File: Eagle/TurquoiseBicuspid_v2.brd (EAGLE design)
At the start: 56 x 56 mm, 19 parts, among them J0 0Ω, J2 0Ω

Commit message: board design v2
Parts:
- moved C2 0.20 mm to (34.7, 46.2)
- moved R5 0.20 mm to (36.9, 46.2)
- moved R2 0.10 mm to (23.9, 34.7)
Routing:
- net GND: track 244.4 -> 299.3 mm
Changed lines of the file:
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@@
 <wire x1="56" y1="56" x2="0" y2="56" width="0" layer="20"/>
 <wire x1="0" y1="56" x2="0" y2="0" width="0" layer="20"/>
-<text x="3.6" y="15.4" size="1.27" layer="21">Jared De La Cruz
+<text x="6.5" y="11.3" size="1.27" layer="21">Jared De La Cruz
 jared@jareddlc.com
 @jareddlc</text>
@@
 <attribute name="MF" value="" x="-28.58" y="11.45" size="1.778" layer="27" rot="R270" display="off"/>
 <attribute name="OC_FARNELL" value="unknown" x="-28.58" y="11.45" size="1.778" layer="27" rot="R270" display="off"/>
-<attribute name="NAME" x="10.765" y="27.235" size="1.27" layer="25"/>
+<attribute name="NAME" x="11.365" y="27.635" size="1.27" layer="25"/>
 </element>
 <element name="R1" library="rcl" package="M1206" value="330Ω" x="23.9" y="31.59" smashed="yes" rot="R180">
-<attribute name="NAME" x="22.67" y="34.22" size="1.27" layer="25" rot="R180"/>
-<attribute name="VALUE" x="27.27" y="34.23" size="1.27" layer="27" rot="R180"/>
-</element>
-<element name="R2" library="rcl" package="M1206" value="330Ω" x="23.9" y="34.6" smashed="yes">
-<attribute name="NAME" x="20.73" y="35.97" size="1.27" layer="25"/>
-<attribute name="VALUE" x="23.53" y="35.96" size="1.27" layer="27"/>
+<attribute name="NAME" x="21.77" y="30.02" size="1.27" layer="25" rot="R180"/>
+<attribute name="VALUE" x="26.17" y="30.03" size="1.27" layer="27" rot="R180"/>
+</element>
+<element name="R2" library="rcl" package="M1206" value="330Ω" x="23.9" y="34.7" smashed="yes">
+<attribute name="NAME" x="19.63" y="32.57" size="1.27" layer="25"/>
+<attribute name="VALUE" x="22.43" y="32.56" size="1.27" layer="27"/>
 </element>
 <element name="R3" library="rcl" package="M1206" value="330Ω" x="32.19" y="33.1" smashed="yes" rot="R90">
-<attribute name="NAME" x="30.77" y="36.72" size="1.27" layer="25" rot="R180"/>
-<attribute name="VALUE" x="35.57" y="36.73" size="1.27" layer="27" rot="R180"/>
+<attribute name="NAME" x="31.07" y="30.52" size="1.27" layer="25" rot="R180"/>
+<attribute name="VALUE" x="35.57" y="30.53" size="1.27" layer="27" rot="R180"/>
 </element>
 <element name="S1" library="switch-omron" package="B3F-10XX" value="" x="6.35" y="4.12">
@@
 </element>
 <element name="R4" library="rcl" package="R1206" value="10kΩ" x="21.61" y="48.55" smashed="yes" rot="R270">
-<attribute name="NAME" x="16.88" y="51.28" size="1.27" layer="25"/>
-<attribute name="VALUE" x="19.28" y="51.27" size="1.27" layer="27"/>
+<attribute name="NAME" x="18.38" y="44.98" size="1.27" layer="25"/>
+<attribute name="VALUE" x="20.88" y="44.97" size="1.27" layer="27"/>
 </element>
 <element name="S2" library="switch-omron" package="B3F-10XX" value="" x="49.72" y="4.12">
@@
 </element>
 <element name="J0" library="rcl" package="R1206" value="0Ω" x="17.31" y="26.4" smashed="yes">
-<attribute name="NAME" x="14.53" y="24.24" size="1.27" layer="25" rot="R90"/>
-<attribute name="VALUE" x="14.54" y="26.64" size="1.27" layer="27" rot="R90"/>
+<attribute name="NAME" x="16.66" y="24.93" size="1.27" layer="25" rot="R180"/>
+<attribute name="VALUE" x="19.26" y="24.84" size="1.27" layer="27" rot="R180"/>
 </element>
 <element name="J2" library="rcl" package="R1206" value="0Ω" x="28" y="50.8" smashed="yes" rot="R90">
-<attribute name="NAME" x="34.17" y="52.53" size="1.27" layer="25" rot="R180"/>
-<attribute name="VALUE" x="36.87" y="52.54" size="1.27" layer="27" rot="R180"/>
-</element>
-<element name="R5" library="resistor" package="R1206" value="10kΩ" x="36.9" y="46" rot="R270"/>
-<element name="R6" library="resistor" package="R1206" value="10kΩ" x="37.9" y="41.1" rot="R270"/>
+<attribute name="NAME" x="27.37" y="47.53" size="1.27" layer="25" rot="R180"/>
+<attribute name="VALUE" x="29.87" y="47.54" size="1.27" layer="27" rot="R180"/>
+</element>
+<element name="R5" library="resistor" package="R1206" value="10kΩ" x="36.9" y="46.2" smashed="yes" rot="R270">
+<attribute name="NAME" x="36.003" y="49.143" size="1.27" layer="25"/>
+<attribute name="VALUE" x="38.403" y="49.187" size="1.27" layer="27"/>
+</element>
+<element name="R6" library="resistor" package="R1206" value="10kΩ" x="37.9" y="41.1" smashed="yes" rot="R270">
+<attribute name="NAME" x="35.203" y="37.243" size="1.27" layer="25"/>
+<attribute name="VALUE" x="35.003" y="35.787" size="1.27" layer="27"/>
+</element>
 <element name="HM-10" library="HM-10" package="HM-10" value="HM-10BOARD" x="47.6" y="41.1"/>
 <element name="USB" library="fci_micro_usb" package="10118192-0001LF" value="10118192-0001LF" x="0" y="30.5" rot="R270"/>
-<element name="ATTINY85" library="attiny85" package="ATTINY85" value="ATTINY85SU" x="28.7" y="40.4" rot="R270"/>
-<element name="C2" library="rcl" package="C1206" value="0.1µf" x="34.7" y="46" rot="R90"/>
-<element name="C3" library="rcl" package="C1206" value="10µf" x="8.7" y="30.5" rot="R270"/>
+<element name="ATTINY85" library="attiny85" package="ATTINY85" value="ATTINY85SU" x="28.7" y="40.4" smashed="yes" rot="R270">
+<attribute name="NAME" x="22.96" y="43.167" size="1.4224" layer="25" ratio="9"/>
+<attribute name="VALUE" x="21.56" y="36.2042" size="1.4224" layer="27" ratio="9"/>
+</element>
+<element name="C2" library="rcl" package="C1206" value="0.1µf" x="34.7" y="46.2" smashed="yes" rot="R90">
+<attribute name="NAME" x="33.37" y="47.53" size="1.27" layer="25" rot="R180"/>
+<attribute name="VALUE" x="33.77" y="46.14" size="1.27" layer="27" rot="R180"/>
+</element>
+<element name="C3" library="rcl" package="C1206" value="10µf" x="8.7" y="30.5" smashed="yes" rot="R270">
+<attribute name="NAME" x="5.03" y="26.67" size="1.27" layer="25"/>
+<attribute name="VALUE" x="7.53" y="26.66" size="1.27" layer="27"/>
+</element>
 </elements>
 <signals>
@@
 <wire x1="11.6" y1="29.1" x2="11.6" y2="30.5" width="0.4064" layer="1"/>
 <wire x1="13.2999" y1="30.5" x2="11.6" y2="30.5" width="0.4064" layer="1"/>
-<wire x1="34.7" y1="47.4" x2="35.1" y2="51.1" width="0.4064" layer="1"/>
-<wire x1="35.1" y1="51.1" x2="35.1" y2="54.6" width="0" layer="19" extent="1-16"/>
-<wire x1="36.9" y1="47.422" x2="38.8" y2="51.1" width="0" layer="19" extent="1-16"/>
-<wire x1="38.8" y1="51.1" x2="35.1" y2="51.1" width="0.4064" layer="1"/>
+<wire x1="34.7" y1="47.6" x2="34.7" y2="50.9" width="0.4064" layer="1"/>
 <wire x1="19.3" y1="26.4" x2="19.3" y2="28.1" width="0.4064" layer="1"/>
 <wire x1="19.3" y1="28.1" x2="19.3" y2="48.5594" width="0.4064" layer="1"/>
@@
 <wire x1="23.9" y1="38.495" x2="23.9" y2="28.1" width="0.4064" layer="1"/>
 <wire x1="23.9" y1="38.495" x2="25.37" y2="38.495" width="0.4064" layer="1"/>
-<wire x1="24.7388" y1="48.5594" x2="34.7" y2="47.4" width="0" layer="19" extent="1-1"/>
+<wire x1="37.9" y1="42.522" x2="38.4" y2="43.122" width="0.4064" layer="1"/>
+<wire x1="38.4" y1="43.122" x2="38.4" y2="50.9" width="0.4064" layer="1"/>
+<wire x1="36.9" y1="47.622" x2="36.9" y2="50.9" width="0.4064" layer="1"/>
+<wire x1="34.7" y1="50.9" x2="36.9" y2="50.9" width="0.4064" layer="1"/>
+<wire x1="36.9" y1="50.9" x2="38.4" y2="50.9" width="0.4064" layer="1"/>
+<wire x1="38.4" y1="50.9" x2="46.8" y2="50.9" width="0.4064" layer="1"/>
+<wire x1="46.8" y1="50.9" x2="46.8" y2="23.1" width="0.4064" layer="1"/>
+<wire x1="46.8" y1="23.1" x2="40.1" y2="23.1" width="0.4064" layer="1"/>
 <wire x1="15.888" y1="26.4" x2="18.732" y2="26.4" width="0" layer="19" extent="1-1"/>
-<wire x1="37.9" y1="42.522" x2="38.4" y2="43.122" width="0.4064" layer="1"/>
-<wire x1="38.4" y1="43.122" x2="38.4" y2="48.5" width="0.4064" layer="1"/>
-<wire x1="38.4" y1="48.5" x2="37.676609375" y2="48.92535" width="0" layer="19" extent="1-16"/>
+<wire x1="46.8" y1="23.1" x2="53.5" y2="23.1" width="0.4064" layer="1"/>
 </signal>
 <signal name="A3">
@@
 <contactref element="R2" pad="2"/>
 <contactref element="ATTINY85" pad="3"/>
-<wire x1="22.5" y1="34.6" x2="21.3" y2="34.6" width="0.4064" layer="1"/>
-<wire x1="21.3" y1="34.6" x2="21.3" y2="39.765" width="0.4064" layer="1"/>
+<wire x1="22.5" y1="34.7" x2="21.3" y2="34.7" width="0.4064" layer="1"/>
+<wire x1="21.3" y1="34.7" x2="21.3" y2="39.765" width="0.4064" layer="1"/>
 <wire x1="21.3" y1="39.765" x2="25.37" y2="39.765" width="0.4064" layer="1"/>
-<wire x1="22.5" y1="34.6" x2="25.3" y2="34.6" width="0" layer="19" extent="1-1"/>
-<wire x1="28.06" y1="29.1" x2="28.06" y2="34.6" width="0.4064" layer="1"/>
-<wire x1="28.06" y1="34.6" x2="25.3" y2="34.6" width="0.4064" layer="1"/>
+<wire x1="22.5" y1="34.7" x2="25.3" y2="34.7" width="0" layer="19" extent="1-1"/>
+<wire x1="28.06" y1="29.1" x2="28.06" y2="34.7" width="0.4064" layer="1"/>
+<wire x1="28.06" y1="34.7" x2="25.3" y2="34.7" width="0.4064" layer="1"/>
 </signal>
 <signal name="3.3V">
@@
 <wire x1="15.9001" y1="31.45" x2="17.3" y2="31.45" width="0.4064" layer="1"/>
 <wire x1="17.3" y1="31.45" x2="17.3" y2="50.9" width="0.4064" layer="1"/>
-<wire x1="34.7" y1="44.6" x2="34.7" y2="42.305" width="0.4064" layer="1"/>
+<wire x1="34.7" y1="44.8" x2="34.7" y2="42.305" width="0.4064" layer="1"/>
 <wire x1="34.7" y1="42.305" x2="32.03" y2="42.305" width="0.4064" layer="1"/>
 <wire x1="40.1" y1="24.6" x2="40.1" y2="24.61" width="0.4064" layer="1"/>
@@
 <wire x1="17.3" y1="50.9" x2="21.61" y2="50.9" width="0.4064" layer="1"/>
 <wire x1="21.61" y1="50.9" x2="33.4" y2="50.9" width="0.4064" layer="1"/>
-<wire x1="33.4" y1="50.9" x2="33.4" y2="44.6" width="0.4064" layer="1"/>
-<wire x1="33.4" y1="44.6" x2="34.7" y2="44.6" width="0.4064" layer="1"/>
+<wire x1="33.4" y1="50.9" x2="33.4" y2="44.8" width="0.4064" layer="1"/>
+<wire x1="33.4" y1="44.8" x2="34.7" y2="44.8" width="0.4064" layer="1"/>
 <wire x1="21.61" y1="49.972" x2="21.61" y2="50.9" width="0.4064" layer="1"/>
 </signal>
@@
 <wire x1="36.4" y1="41.1" x2="32.03" y2="41.1" width="0.4064" layer="1"/>
 <wire x1="32.03" y1="41.1" x2="32.03" y2="41.035" width="0.4064" layer="1"/>
-<wire x1="36.9" y1="44.578" x2="36.4" y2="43.878" width="0.4064" layer="1"/>
+<wire x1="36.9" y1="44.778" x2="36.4" y2="43.878" width="0.4064" layer="1"/>
 <wire x1="36.4" y1="43.878" x2="36.4" y2="41.1" width="0.4064" layer="1"/>
 </signal>

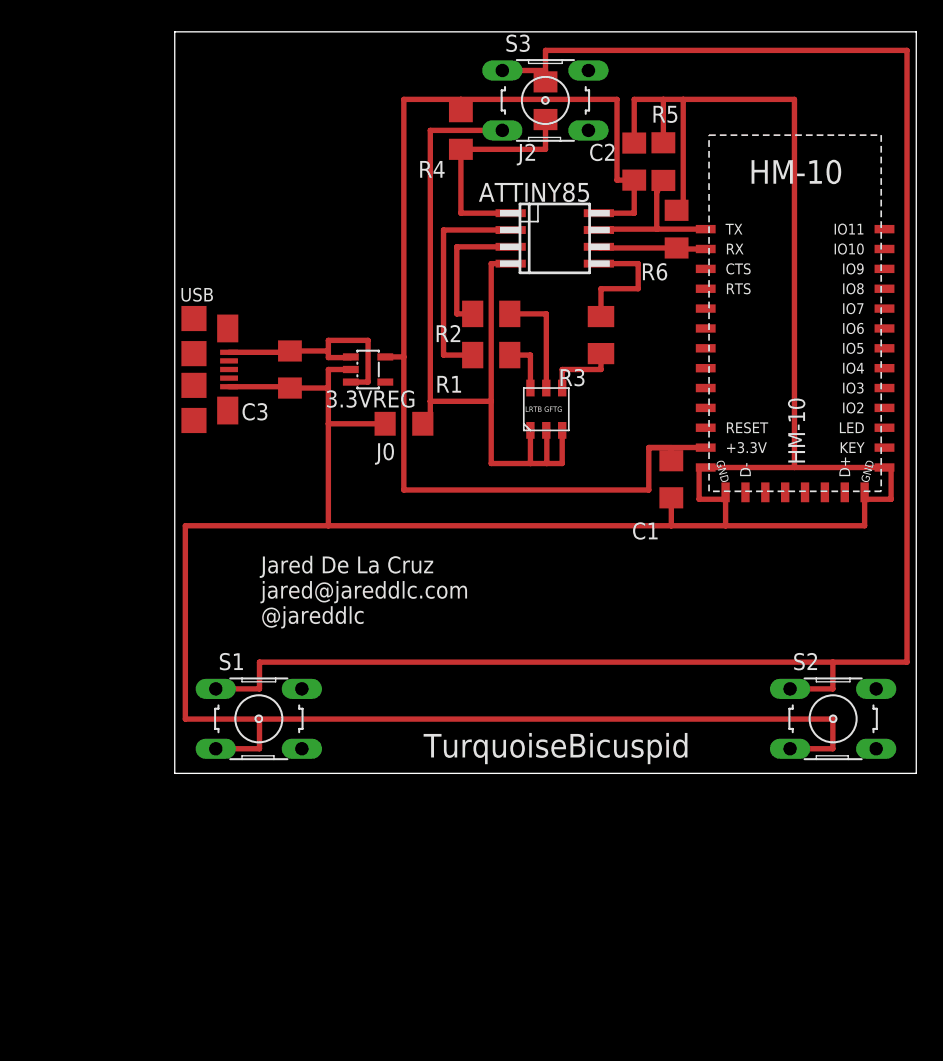
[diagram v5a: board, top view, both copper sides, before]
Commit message: added miter bends
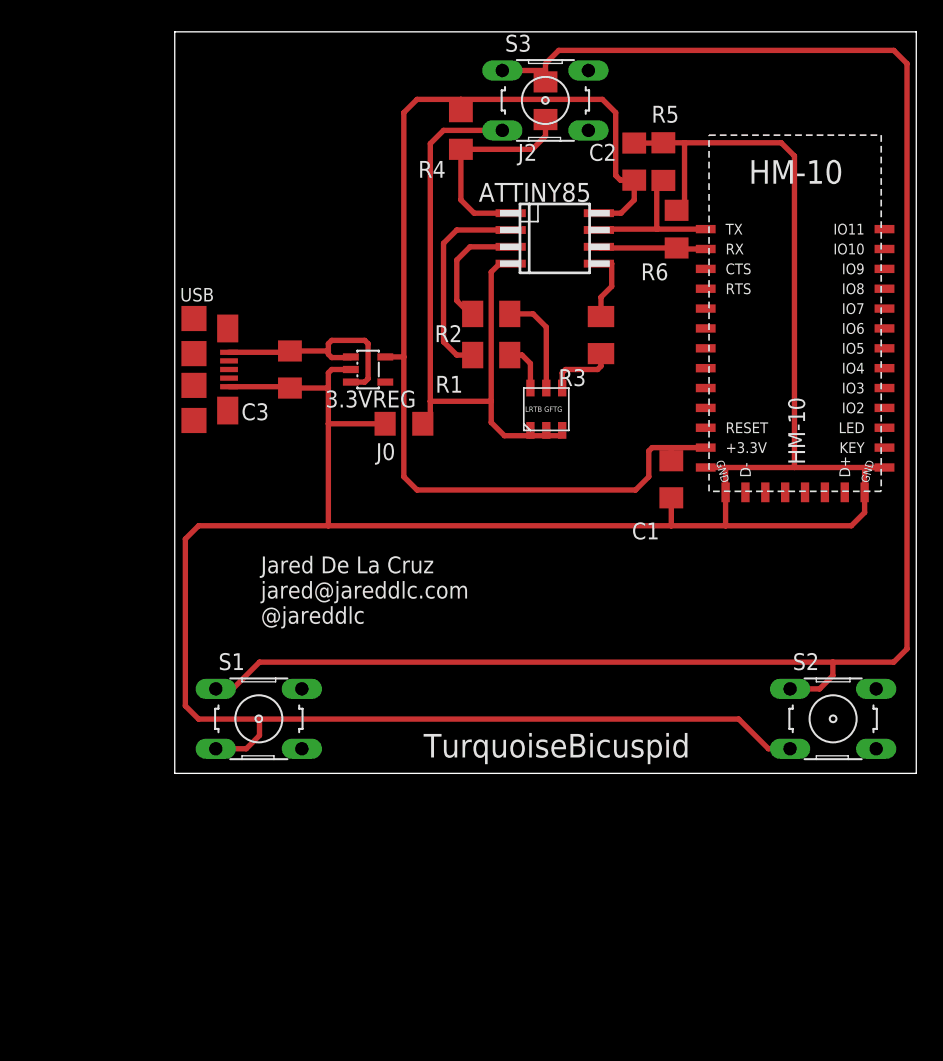
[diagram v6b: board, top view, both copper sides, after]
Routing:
- net GND: track 299.3 -> 258.1 mm
- net 3.3V: track 89.2 -> 84.2 mm
- net A3: track 15.3 -> 10.5 mm
- net RESET: track 156.7 -> 152.0 mm
- net N$1: track 0.00 -> 2.30 mm
- net A2: track 18.7 -> 17.1 mm
- net A1: track 20.8 -> 19.2 mm
- net 5V: track 18.0 -> 17.4 mm
